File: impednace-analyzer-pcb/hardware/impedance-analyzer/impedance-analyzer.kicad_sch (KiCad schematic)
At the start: 11 parts, among them J1 AD9833, J2 ADS1256_SPI, J3 ADS1256_AIN, J4 UNO_POWER, J5 UNO_ANALOG, J6 UNO_DIGITAL_LOW, J7 UNO_DIGITAL_HIGH, J8 PIEZO

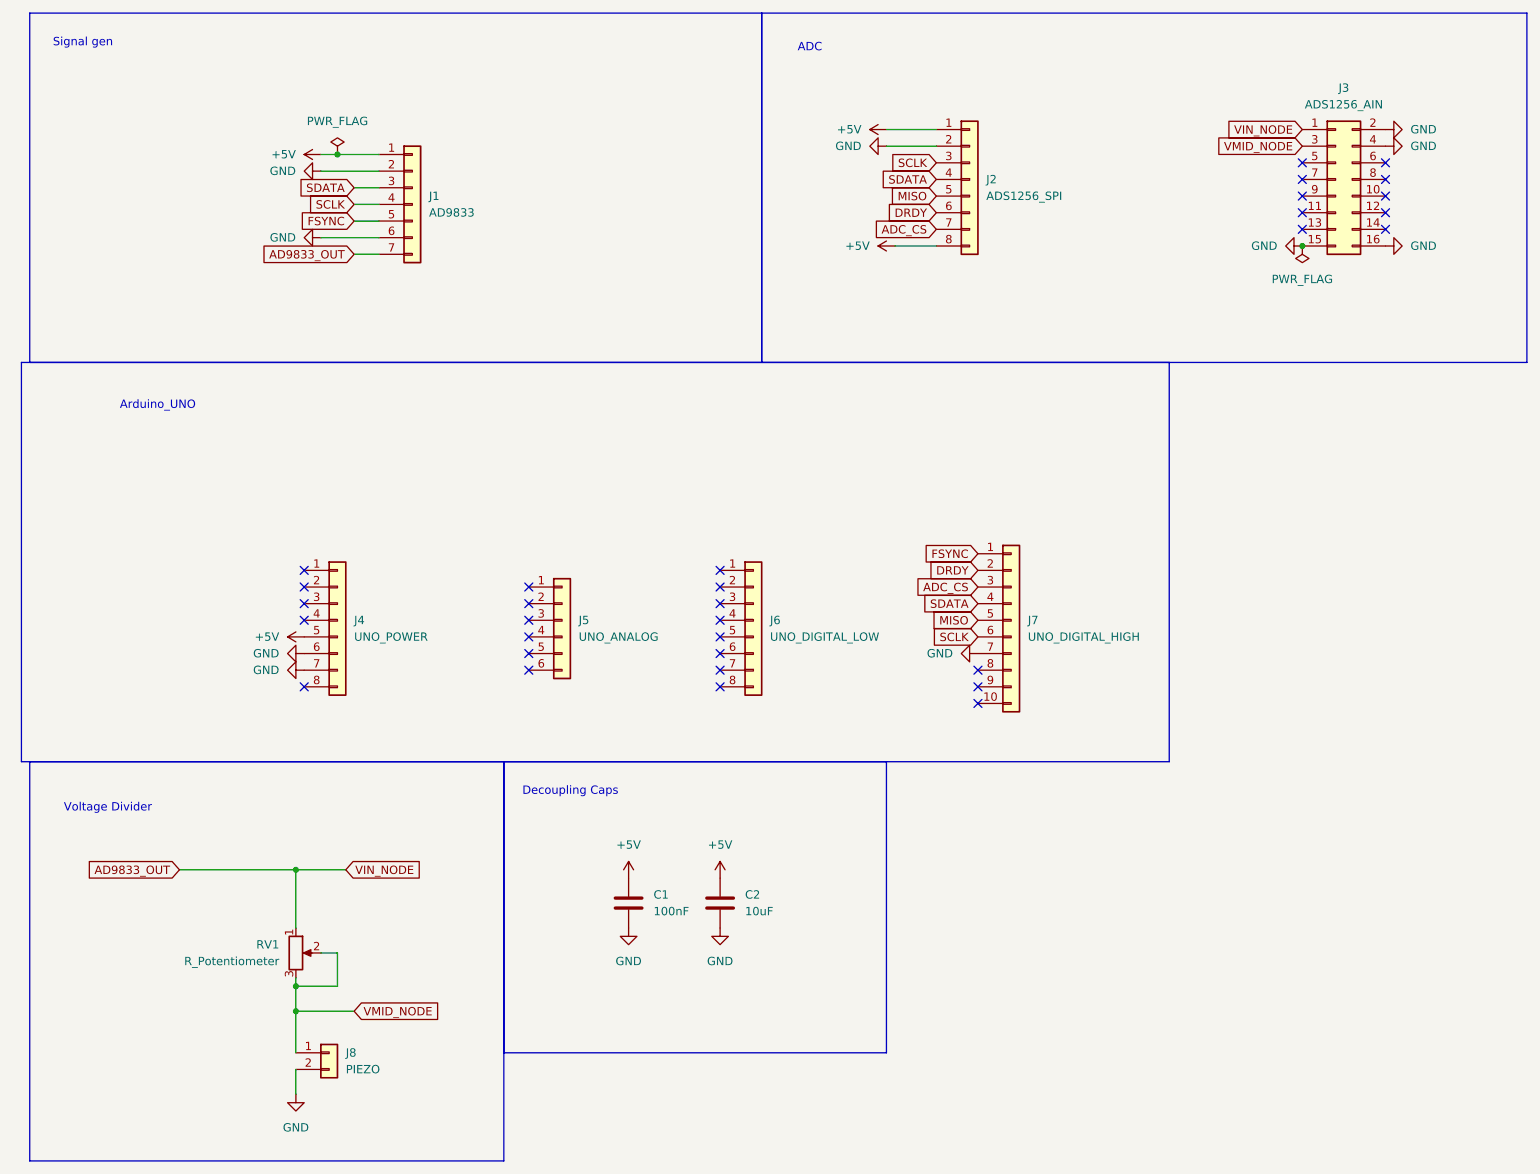
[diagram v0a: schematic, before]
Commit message: added mux and jack to schematic
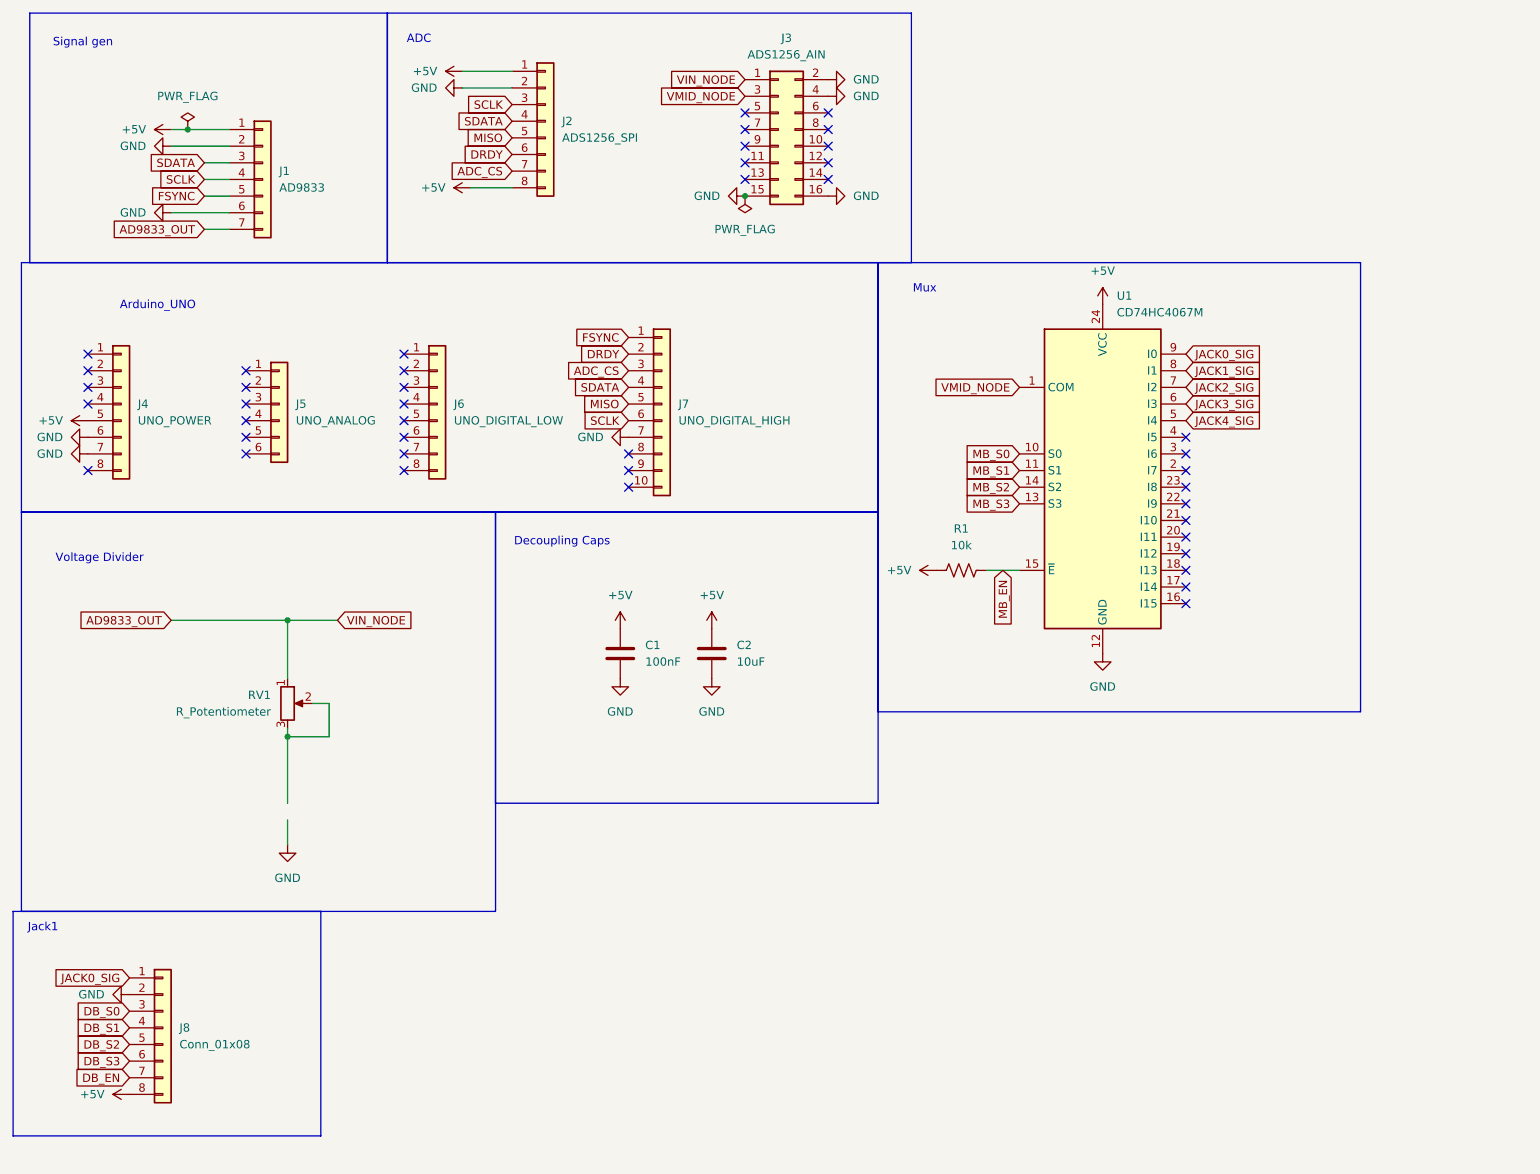
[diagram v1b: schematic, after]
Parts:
- removed J8: PIEZO, TerminalBlock:TerminalBlock_MaiXu_MX126-5.0-02P_1x02_P5.00mm, symbol Connector_Generic:Conn_01x02
- added J8: Conn_01x08, symbol Connector_Generic:Conn_01x08
- added R1: 10k, symbol Device:R_US
- added U1: CD74HC4067M, Package_SO:SOIC-24W_7.5x15.4mm_P1.27mm, symbol 74xx:CD74HC4067M
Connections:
- net +5V: now also J8.8 (Pin_8), R1.1, U1.24 (VCC)
- net GND: now also J8.2 (Pin_2), U1.12 (GND)
- net VMID_NODE: now also U1.1 (COM); no longer RV1.2, RV1.3
- new net: RV1.2, RV1.3
- new net DB_EN: J8.7 (Pin_7)
- new net DB_S0: J8.3 (Pin_3)
- new net DB_S1: J8.4 (Pin_4)
- new net DB_S2: J8.5 (Pin_5)
- new net DB_S3: J8.6 (Pin_6)
- new net JACK0_SIG: J8.1 (Pin_1), U1.9 (I0)
- new net JACK1_SIG: U1.8 (I1)
- new net JACK2_SIG: U1.7 (I2)
- new net JACK3_SIG: U1.6 (I3)
- new net JACK4_SIG: U1.5 (I4)
- new net MB_EN: R1.2, U1.15 (~{E})
- new net MB_S0: U1.10 (S0)
- new net MB_S1: U1.11 (S1)
- new net MB_S2: U1.14 (S2)
- new net MB_S3: U1.13 (S3)
- no-connect marks 32 -> 43
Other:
- note added: "Jack1"
- note added: "Mux"
- moved on the sheet: C1, C2, J1, J2, J3, J4, J5, J6, J7, RV1

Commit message: updated schematic
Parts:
- added J10, J11, J12, J9: Conn_01x08, Connector_Molex:Molex_Micro-Fit_3.0_43650-0815_1x08_P3.00mm_Vertical, symbol Connector_Generic:Conn_01x08
- J8: footprint (none) -> Connector_Molex:Molex_Micro-Fit_3.0_43650-0815_1x08_P3.00mm_Vertical
- R1: footprint (none) -> Resistor_SMD:R_0805_2012Metric_Pad1.20x1.40mm_HandSolder
- U1: footprint Package_SO:SOIC-24W_7.5x15.4mm_P1.27mm -> Package_DIP:DIP-24_W7.62mm
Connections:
- net +5V: now also J10.8 (Pin_8), J11.8 (Pin_8), J12.8 (Pin_8), J9.8 (Pin_8)
- net AD9833_OUT: now also J3.2 (Pin_2); no longer J3.1 (Pin_1)
- net DB_EN: now also J5.4 (Pin_4), J10.7 (Pin_7), J11.7 (Pin_7), J12.7 (Pin_7), J9.7 (Pin_7)
- net DB_S0: now also J6.8 (Pin_8), J10.3 (Pin_3), J11.3 (Pin_3), J12.3 (Pin_3), J9.3 (Pin_3)
- net DB_S1: now also J5.1 (Pin_1), J10.4 (Pin_4), J11.4 (Pin_4), J12.4 (Pin_4), J9.4 (Pin_4)
- net DB_S2: now also J5.2 (Pin_2), J10.5 (Pin_5), J11.5 (Pin_5), J12.5 (Pin_5), J9.5 (Pin_5)
- net DB_S3: now also J5.3 (Pin_3), J10.6 (Pin_6), J11.6 (Pin_6), J12.6 (Pin_6), J9.6 (Pin_6)
- net GND: now also J3.1 (Pin_1), J3.10 (Pin_10), J3.11 (Pin_11), J3.12 (Pin_12), J3.13 (Pin_13), J3.14 (Pin_14), J3.3 (Pin_3), J3.5 (Pin_5), J3.6 (Pin_6), J3.7 (Pin_7), J3.8 (Pin_8), J3.9 (Pin_9), J10.2 (Pin_2), J11.2 (Pin_2), J12.2 (Pin_2), J9.2 (Pin_2); no longer J3.2 (Pin_2), J3.4 (Pin_4)
- net JACK1_SIG: now also J9.1 (Pin_1)
- net JACK2_SIG: now also J10.1 (Pin_1)
- net JACK3_SIG: now also J11.1 (Pin_1)
- net JACK4_SIG: now also J12.1 (Pin_1)
- net MB_EN: now also J6.7 (Pin_7)
- net MB_S0: now also J6.3 (Pin_3)
- net MB_S1: now also J6.4 (Pin_4)
- net MB_S2: now also J6.5 (Pin_5)
- net MB_S3: now also J6.6 (Pin_6)
- net VMID_NODE: now also J3.4 (Pin_4), RV1.2, RV1.3; no longer J3.3 (Pin_3)
- no-connect marks 43 -> 23
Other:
- note added: "Jack2"
- note added: "Jack3"
- note added: "Jack4"
- note added: "Jack5"
- moved on the sheet: C1, C2, J8, R1, RV1, U1
